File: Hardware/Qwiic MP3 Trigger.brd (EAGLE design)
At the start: 25.4 x 50.8 mm, 104 parts, among them J1 MICRO-SD, J3 PTH, J7 ISP, J8 3.5mm Audio, J9 Poke-Home, U1 TPA2005D1, U2 WT2003S, U3 AP2112-3.3V, U4 ATTINY84-ARDUINO

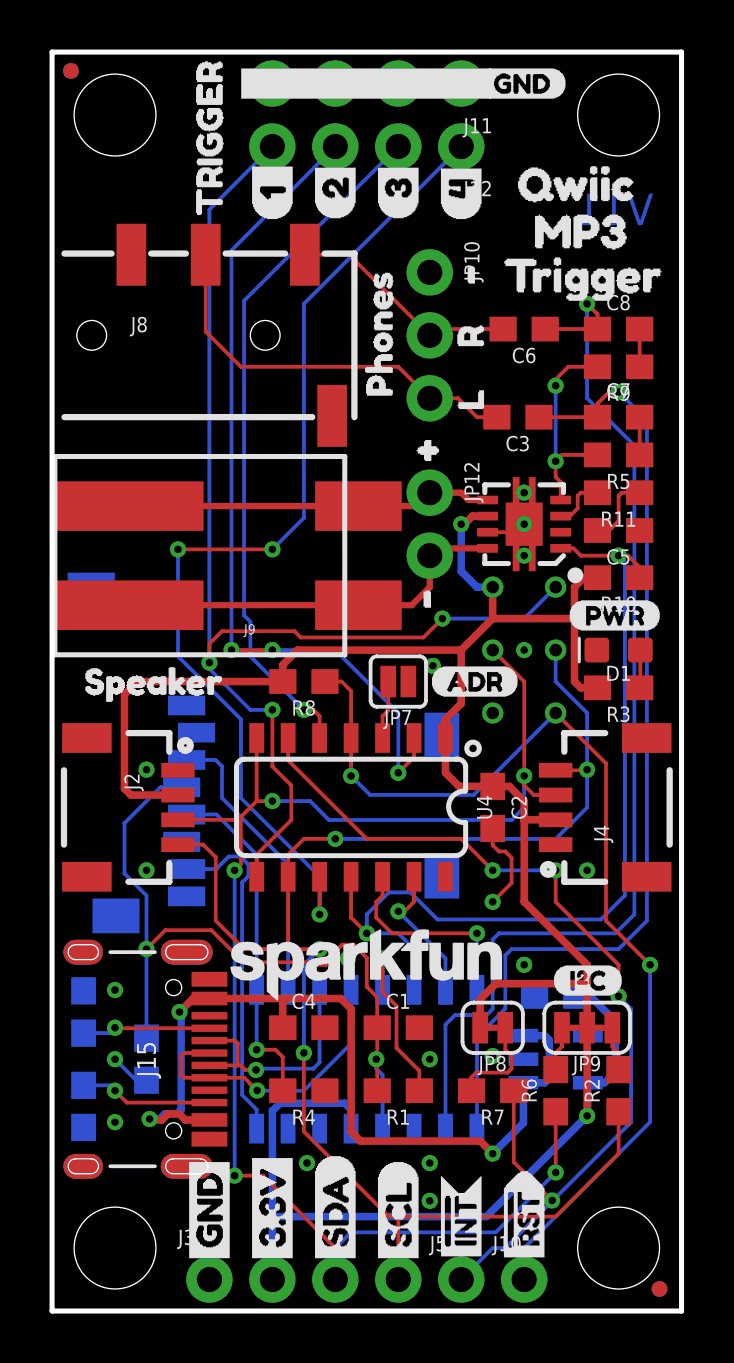
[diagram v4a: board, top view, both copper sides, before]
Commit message: Re-route to accommodate H4
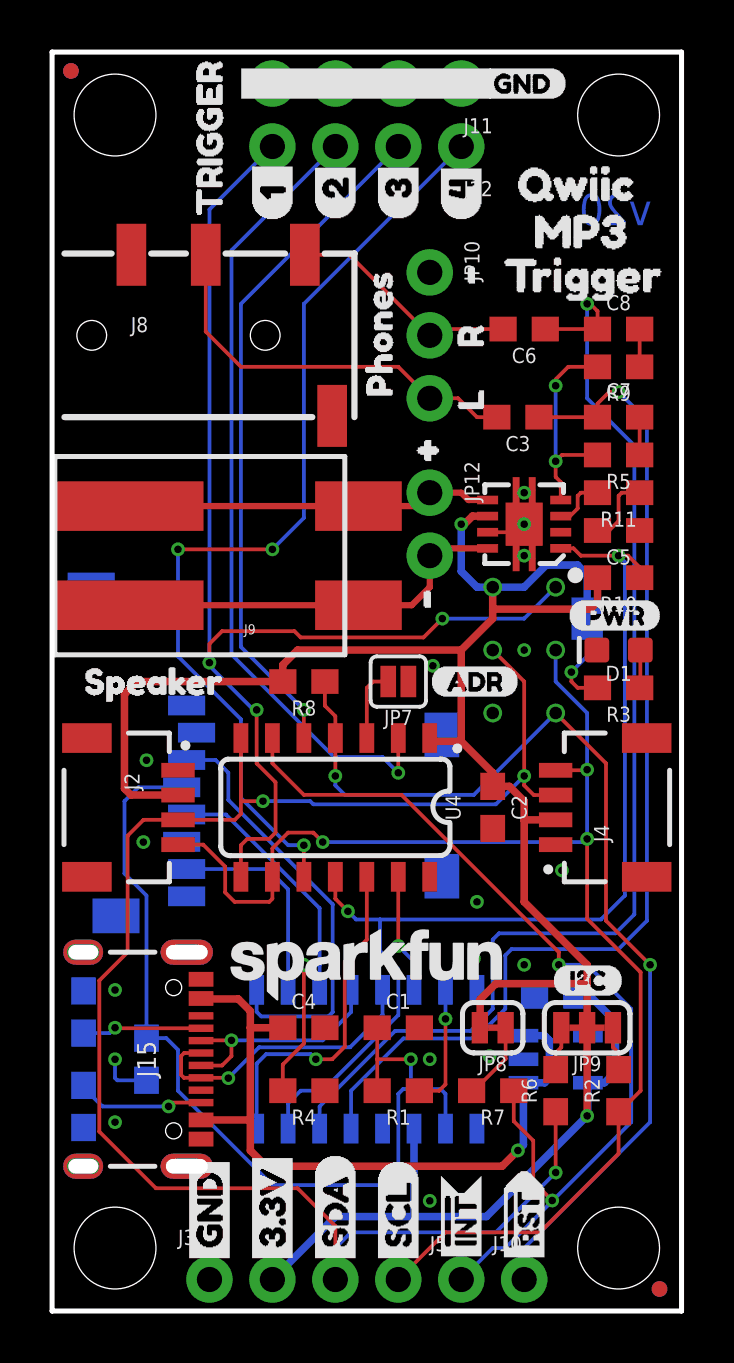
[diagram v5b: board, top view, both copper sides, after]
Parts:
- removed U2: WT2003S, WT2003S:SO16
- added JP14: JUMPER-SMT_2_NC_TRACE_SILK, SparkFun-Jumpers:SMT-JUMPER_2_NC_TRACE_SILK
- added U$2: (no value), output:#PWR#0
- added U5: WT2003SH4, SparkFun-IC-Special-Function:SO16
- J15: device SparkFun-Connectors:USB-C-16P -> SparkFun-Connectors:USB-C-16P-2LAYER-PADS
- J2, J4: value (none) -> QWIIC_RIGHT_ANGLE; device SparkFun-Connectors:1X04_1MM_RA -> SparkFun-Connectors:JST04_1MM_RA
- JP9: value (none) -> JUMPER-SMT_3_2-NC_TRACE_SILK
- moved U4 1.27 mm to (11.4, 20.3)
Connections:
- removed net !SDN: U2.7
- new net N$6: JP14.1, R3.2
- net 3.3V: now also JP14.2, U5.11; no longer R3.2, U2.5
- net ADKEY: now also U5.7; no longer U2.13
- net D+: now also U5.5; no longer U2.12
- net D-: now also U5.4; no longer U2.11
- net GND: now also U5.12, U5.8; no longer J15.SHLD5, J15.SHLD6, J15.SHLD7, J15.SHLD8, U2.3, U2.6
- net MP3-RXI: now also U5.6; no longer U2.15
- net MP3-TXO: now also U5.16; no longer U2.16
- net PLAYING: now also U5.15; no longer U2.14
- net SD_CLK: now also U5.3; no longer U2.9
- net SD_CMD: now also U5.1; no longer U2.10
- net SD_DAT: now also U5.2; no longer U2.8
- net VCCIO: now also U5.10; no longer U2.4
- net VOUTL: now also U5.13; no longer U2.1
- net VOUTR: now also U5.14; no longer U2.2
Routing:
- net VCCIO: track 30.9 -> 37.9 mm, vias 2 -> 1
- net SDA: track 61.0 -> 66.9 mm, vias 5 -> 3
- net SCL: track 60.8 -> 55.0 mm, vias 4 -> 3
- net SD_CMD: track 11.7 -> 17.4 mm
- net PLAYING: track 36.5 -> 42.2 mm
- net 5V: track 34.7 -> 29.1 mm, vias 3 -> 1
- net MP3-TXO: track 8.36 -> 13.9 mm
- net SD_DAT: track 13.8 -> 8.49 mm
- net 3.3V: track 99.6 -> 94.9 mm
- net VOUTL: track 39.5 -> 43.3 mm
- net N$6: track 0.00 -> 3.44 mm, vias 0 -> 1
- net GND: track 8.47 -> 5.17 mm, vias 19 -> 17
- net VOUTR: track 44.0 -> 47.2 mm
- net TRIGGER4: track 41.8 -> 38.9 mm
- net SD_CLK: track 13.9 -> 16.3 mm
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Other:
- board text added: "v20"
- board text removed: "V11"

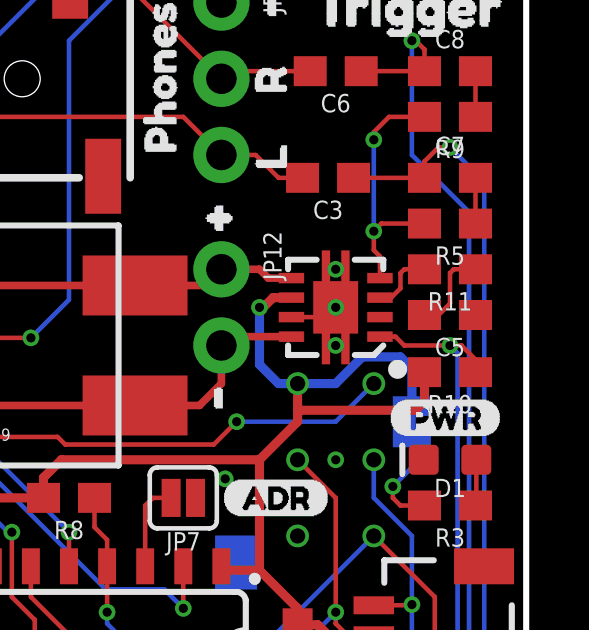
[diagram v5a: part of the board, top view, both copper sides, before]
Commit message: Add pop reduction component changes from v12.
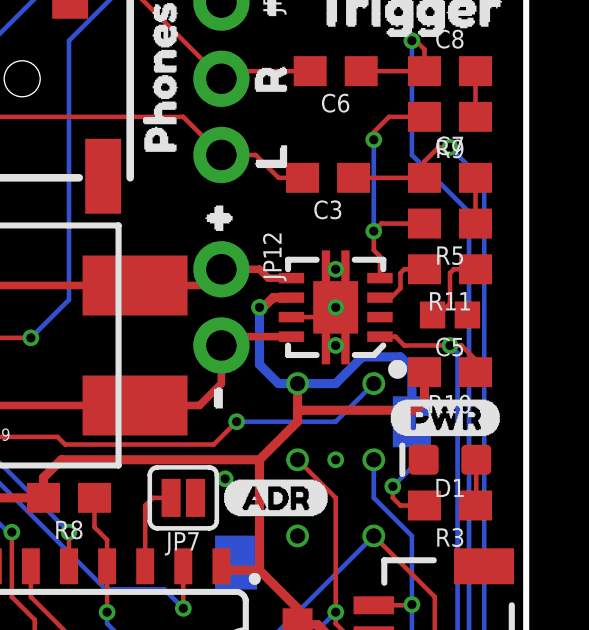
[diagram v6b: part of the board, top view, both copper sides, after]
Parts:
- C5: value 1.0uF -> 22nF; device SparkFun-Capacitors:0603 -> SparkFun-Capacitors:0402
- C7, C8: value 0.1uF -> 10nF
- R11: value 100k -> 47k
- R5, R9: value 10k -> 100k
- R8: value 4.7k -> 10k
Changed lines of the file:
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@@
 <layer number="44" name="Drills" color="7" fill="1" visible="no" active="yes"/>
 <layer number="45" name="Holes" color="7" fill="1" visible="yes" active="yes"/>
-<layer number="46" name="Milling" color="3" fill="1" visible="yes" active="yes"/>
+<layer number="46" name="Milling" color="3" fill="1" visible="no" active="yes"/>
 <layer number="47" name="Measures" color="7" fill="1" visible="no" active="yes"/>
 <layer number="48" name="Document" color="7" fill="1" visible="no" active="yes"/>
@@
 <layer number="95" name="Names" color="7" fill="1" visible="no" active="no"/>
 <layer number="96" name="Values" color="7" fill="1" visible="no" active="no"/>
-<layer number="2" name="Route2" color="1" fill="3" visible="yes" active="yes"/>
-<layer number="15" name="Route15" color="4" fill="6" visible="yes" active="yes"/>
+<layer number="2" name="Route2" color="1" fill="3" visible="no" active="yes"/>
+<layer number="15" name="Route15" color="4" fill="6" visible="no" active="yes"/>
 <layer number="3" name="Route3" color="4" fill="3" visible="no" active="no"/>
 <layer number="4" name="Route4" color="1" fill="4" visible="no" active="no"/>
@@
 <attribute name="VALUE" x="21.082" y="8.89" size="0.6096" layer="27" font="vector" ratio="20" rot="R90" align="top-center"/>
 </element>
-<element name="R8" library="SparkFun-Resistors" package="0603" value="4.7k" x="10.16" y="25.4" smashed="yes" rot="R180">
+<element name="R8" library="SparkFun-Resistors" package="0603" value="10k" x="10.16" y="25.4" smashed="yes" rot="R180">
 <attribute name="NAME" x="10.16" y="24.638" size="0.6096" layer="25" font="vector" ratio="20" rot="R180" align="bottom-center"/>
-<attribute name="PROD_ID" value="RES-07857" x="53.34" y="33.02" size="1.778" layer="27" font="vector" ratio="15" rot="R180" display="off"/>
-<attribute name="VALUE" x="12.573" y="25.146" size="0.6096" layer="27" font="vector" ratio="20" rot="R180" align="top-center"/>
+<attribute name="PROD_ID" value="RES-00824" x="53.34" y="33.02" size="1.778" layer="27" font="vector" ratio="15" rot="R180" display="off"/>
+<attribute name="VALUE" value="10k" x="12.573" y="25.146" size="0.6096" layer="27" font="vector" ratio="20" rot="R180" align="top-center"/>
 </element>
 <element name="J10" library="SparkFun-Connectors" package="1X01_NO_SILK" value="" x="19.05" y="1.27" smashed="yes">
@@
 <attribute name="VALUE" value="10k" x="22.86" y="29.591" size="1.778" layer="27" rot="R180" display="off"/>
 </element>
-<element name="R11" library="SparkFun-Resistors" package="0603" value="100k" x="22.86" y="33.02" smashed="yes" rot="R180">
+<element name="R11" library="SparkFun-Resistors" package="0603" value="47k" x="22.86" y="33.02" smashed="yes" rot="R180">
 <attribute name="NAME" x="22.86" y="32.258" size="0.6096" layer="25" font="vector" ratio="20" rot="R180" align="bottom-center"/>
-<attribute name="PROD_ID" value="RES-07828" x="22.86" y="33.02" size="1.778" layer="27" rot="R180" display="off"/>
-<attribute name="VALUE" value="100k" x="25.4" y="32.766" size="0.6096" layer="27" font="vector" ratio="20" rot="R180" align="top-center"/>
+<attribute name="PROD_ID" value="RES-07871" x="22.86" y="33.02" size="1.778" layer="27" rot="R180" display="off"/>
+<attribute name="VALUE" value="47k" x="25.4" y="32.766" size="0.6096" layer="27" font="vector" ratio="20" rot="R180" align="top-center"/>
 <attribute name="VALUE" value="4.7k" x="22.86" y="33.02" size="1.778" layer="27" rot="R180" display="off"/>
 </element>
@@
 <attribute name="VALUE" x="7.493" y="8.636" size="0.6096" layer="27" font="vector" ratio="20" rot="R180" align="top-center"/>
 </element>
-<element name="R5" library="SparkFun-Resistors" package="0603" value="10k" x="22.86" y="34.544" smashed="yes" rot="R180">
+<element name="R5" library="SparkFun-Resistors" package="0603" value="100k" x="22.86" y="34.544" smashed="yes" rot="R180">
 <attribute name="NAME" x="22.86" y="33.782" size="0.6096" layer="25" font="vector" ratio="20" rot="R180" align="bottom-center"/>
-<attribute name="PROD_ID" value="RES-00824" x="22.86" y="34.544" size="1.778" layer="27" font="vector" ratio="15" rot="R180" display="off"/>
-<attribute name="VALUE" x="25.273" y="34.163" size="0.6096" layer="27" font="vector" ratio="20" rot="R180" align="top-center"/>
-</element>
-<element name="R9" library="SparkFun-Resistors" package="0603" value="10k" x="22.86" y="38.1" smashed="yes" rot="R180">
+<attribute name="PROD_ID" value="RES-07828" x="22.86" y="34.544" size="1.778" layer="27" font="vector" ratio="15" rot="R180" display="off"/>
+<attribute name="VALUE" value="100k" x="25.273" y="34.163" size="0.6096" layer="27" font="vector" ratio="20" rot="R180" align="top-center"/>
+</element>
+<element name="R9" library="SparkFun-Resistors" package="0603" value="100k" x="22.86" y="38.1" smashed="yes" rot="R180">
 <attribute name="NAME" x="22.86" y="37.338" size="0.6096" layer="25" font="vector" ratio="20" rot="R180" align="bottom-center"/>
-<attribute name="PROD_ID" value="RES-00824" x="22.86" y="38.1" size="1.778" layer="27" font="vector" ratio="15" rot="R180" display="off"/>
-<attribute name="VALUE" x="25.273" y="37.846" size="0.6096" layer="27" font="vector" ratio="20" rot="R180" align="top-center"/>
+<attribute name="PROD_ID" value="RES-07828" x="22.86" y="38.1" size="1.778" layer="27" font="vector" ratio="15" rot="R180" display="off"/>
+<attribute name="VALUE" value="100k" x="25.273" y="37.846" size="0.6096" layer="27" font="vector" ratio="20" rot="R180" align="top-center"/>
 </element>
 <element name="U1" library="SparkFun-IC-Amplifiers" package="QFN-8_PAD" value="TPA2005D1" x="19.05" y="31.75" smashed="yes" rot="R90">
@@
 <attribute name="VALUE" value="TPA2005D1" x="19.05" y="31.75" size="1.778" layer="27" rot="R90" display="off"/>
 </element>
-<element name="C7" library="SparkFun-Capacitors" package="0603" value="0.1uF" x="22.86" y="36.068" smashed="yes">
+<element name="C7" library="SparkFun-Capacitors" package="0603" value="10nF" x="22.86" y="36.068" smashed="yes">
 <attribute name="NAME" x="22.86" y="36.83" size="0.6096" layer="25" font="vector" ratio="20" align="bottom-center"/>
-<attribute name="PROD_ID" value="CAP-00810" x="22.86" y="36.068" size="1.778" layer="27" font="vector" ratio="15" display="off"/>
-<attribute name="VALUE" x="25.781" y="36.449" size="0.6096" layer="27" font="vector" ratio="20" align="top-center"/>
-</element>
-<element name="C8" library="SparkFun-Capacitors" package="0603" value="0.1uF" x="22.86" y="39.624" smashed="yes">
+<attribute name="PROD_ID" value="CAP-00867" x="22.86" y="36.068" size="1.778" layer="27" font="vector" ratio="15" display="off"/>
+<attribute name="VALUE" value="10nF" x="25.781" y="36.449" size="0.6096" layer="27" font="vector" ratio="20" align="top-center"/>
+</element>
+<element name="C8" library="SparkFun-Capacitors" package="0603" value="10nF" x="22.86" y="39.624" smashed="yes">
 <attribute name="NAME" x="22.86" y="40.386" size="0.6096" layer="25" font="vector" ratio="20" align="bottom-center"/>
-<attribute name="PROD_ID" value="CAP-00810" x="22.86" y="39.624" size="1.778" layer="27" font="vector" ratio="15" display="off"/>
-<attribute name="VALUE" x="25.908" y="40.005" size="0.6096" layer="27" font="vector" ratio="20" align="top-center"/>
+<attribute name="PROD_ID" value="CAP-00867" x="22.86" y="39.624" size="1.778" layer="27" font="vector" ratio="15" display="off"/>
+<attribute name="VALUE" value="10nF" x="25.908" y="40.005" size="0.6096" layer="27" font="vector" ratio="20" align="top-center"/>
 </element>
 <element name="J11" library="SparkFun-Connectors" package="1X04_NO_SILK" value="" x="16.51" y="49.53" smashed="yes" rot="R180">
@@
 <attribute name="VALUE" x="17.78" y="49.022" size="0.6096" layer="27" font="vector" ratio="20" rot="R180"/>
 </element>
-<element name="C5" library="SparkFun-Capacitors" package="0603" value="1.0uF" x="22.86" y="31.496" smashed="yes" rot="R180">
+<element name="C5" library="SparkFun-Capacitors" package="0402" value="22nF" x="22.86" y="31.496" smashed="yes" rot="R180">
 <attribute name="NAME" x="22.86" y="30.734" size="0.6096" layer="25" font="vector" ratio="20" rot="R180" align="bottom-center"/>
-<attribute name="PROD_ID" value="CAP-00868" x="22.86" y="31.496" size="1.778" layer="27" font="vector" ratio="15" rot="R180" display="off"/>
-<attribute name="VALUE" x="25.654" y="31.242" size="0.6096" layer="27" font="vector" ratio="20" rot="R180" align="top-center"/>
+<attribute name="PROD_ID" value="CAP-15062" x="22.86" y="31.496" size="1.778" layer="27" font="vector" ratio="15" rot="R180" display="off"/>
+<attribute name="VALUE" value="22nF" x="25.654" y="31.242" size="0.6096" layer="27" font="vector" ratio="20" rot="R180" align="top-center"/>
 </element>
 <element name="JP7" library="SparkFun-Jumpers" package="SMT-JUMPER_2_NO_SILK" package3d_urn="urn:adsk.eagle:package:39279/1" value="ADR" x="13.97" y="25.4" smashed="yes" rot="R180">
@@
 <wire x1="15.367" y1="26.035" x2="17.78" y2="24.13" width="0" layer="19" extent="1-1"/>
 <wire x1="14.3764" y1="25.4" x2="15.367" y2="26.035" width="0" layer="19" extent="1-1"/>
-<wire x1="23.71" y1="31.496" x2="19.375" y2="30.3625" width="0" layer="19" extent="1-1"/>
+<wire x1="23.44" y1="31.496" x2="19.375" y2="30.3625" width="0" layer="19" extent="1-1"/>
 <wire x1="17.78" y1="19.47" x2="17.78" y2="24.13" width="0" layer="19" extent="1-1"/>
 <wire x1="20.32" y1="18.82" x2="17.78" y2="19.47" width="0" layer="19" extent="1-1"/>
@@
 <wire x1="22.86" y1="32.893" x2="22.86" y2="31.877" width="0.1524" layer="1"/>
 <wire x1="22.86" y1="31.877" x2="22.479" y2="31.496" width="0.1524" layer="1"/>
-<wire x1="22.479" y1="31.496" x2="22.01" y2="31.496" width="0.1524" layer="1"/>
+<wire x1="22.479" y1="31.496" x2="22.28" y2="31.496" width="0.1524" layer="1"/>
 </signal>
 <signal name="N$9">

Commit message: v20 small test panel
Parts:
- moved U4 0.63 mm to (12.1, 20.3)
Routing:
- net !RST: track 41.3 -> 42.2 mm
- net TRIGGER1: track 48.7 -> 47.9 mm
- net 3.3V: track 94.9 -> 94.2 mm
- net ADR: track 2.99 -> 2.40 mm
